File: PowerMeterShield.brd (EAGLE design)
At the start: 71.1 x 53.3 mm, 35 parts, among them U1 INA170EA/2K5, U2 THS4521, U3 INA138, U4 ADUM1250ARZ, U5 MCP3426A0-E/SN, U6 ISL21080

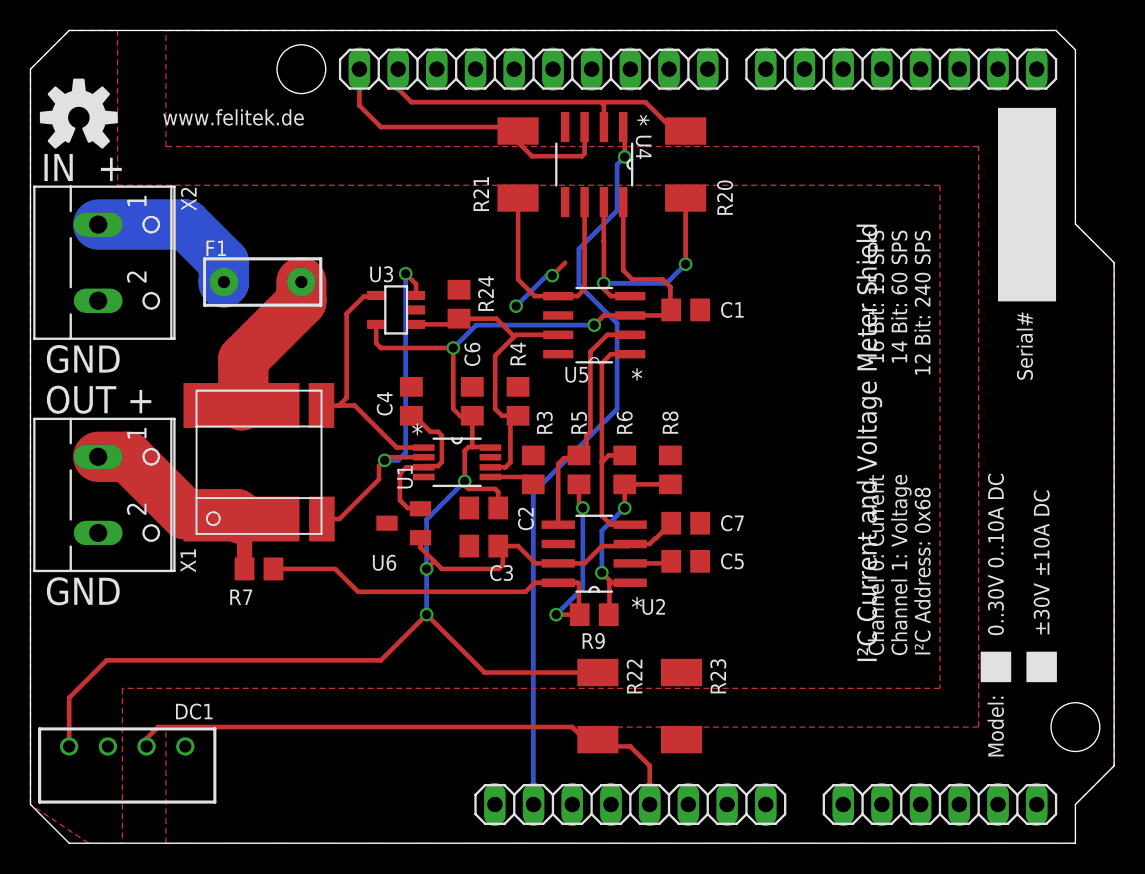
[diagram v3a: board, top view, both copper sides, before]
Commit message: In/Out Sockets conflict with some Arduino's USB/Power jacks, added keepout regions and moved the jacks Reworked the traces from the inputs/outputs to be polygons, thanks moemoe!
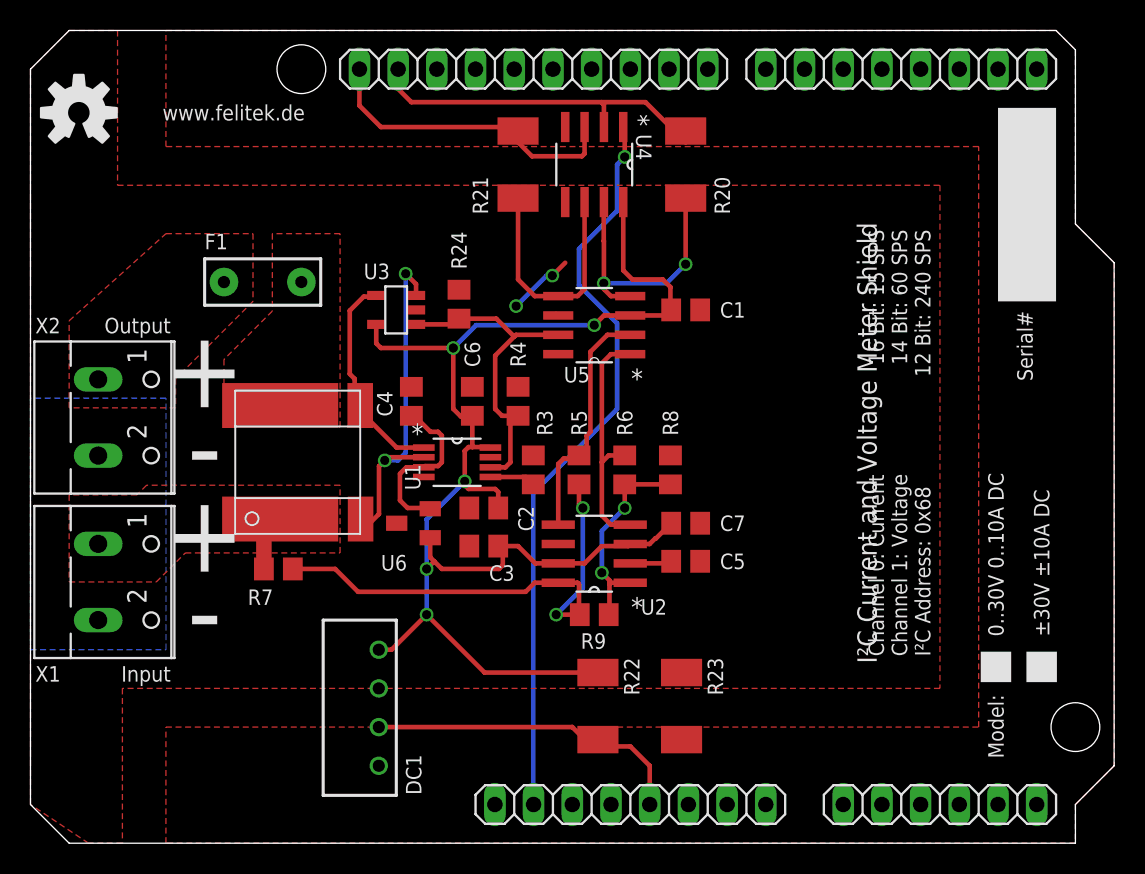
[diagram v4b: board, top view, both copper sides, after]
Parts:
- moved DC1 16.7 mm to (22.9, 8.89), turned to 90 degrees
- moved X2 10.2 mm to (5.71, 27.9)
- moved X1 5.71 mm to (5.71, 17.1)
- moved R1 2.54 mm to (17.5, 25.0)
- moved R7 1.27 mm to (16.3, 18.0)
- moved U6 0.64 mm to (25.1, 21.0)
- moved U$1 0.32 mm to (3.17, 47.9)
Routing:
- net +5V/2: track 119.7 -> 94.6 mm
- net +5V: track 38.1 -> 22.0 mm
- net V_MEAS: track 14.5 -> 3.07 mm
- net VIN_MEAS: track 10.6 -> 0.00 mm
- net N$3: track 9.73 -> 0.00 mm
- net CURRENT-: track 16.5 -> 14.6 mm
- net N$2: track 33.9 -> 32.6 mm
- net CURRENT+: track 23.9 -> 23.0 mm
- net REF: track 10.7 -> 11.3 mm
- added copper zone on layer 16, net GNDI
- added copper zone on layer 1, net N$3
- added copper zone on layer 1, net VIN_MEAS
- added copper zone on layer 1, net V_MEAS
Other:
- board text added: "+"
- board text added: "-"
- board text added: "Input"
- board text added: "Output"
- board text removed: "GND"
- board text removed: "IN +"
- board text removed: "OUT +"

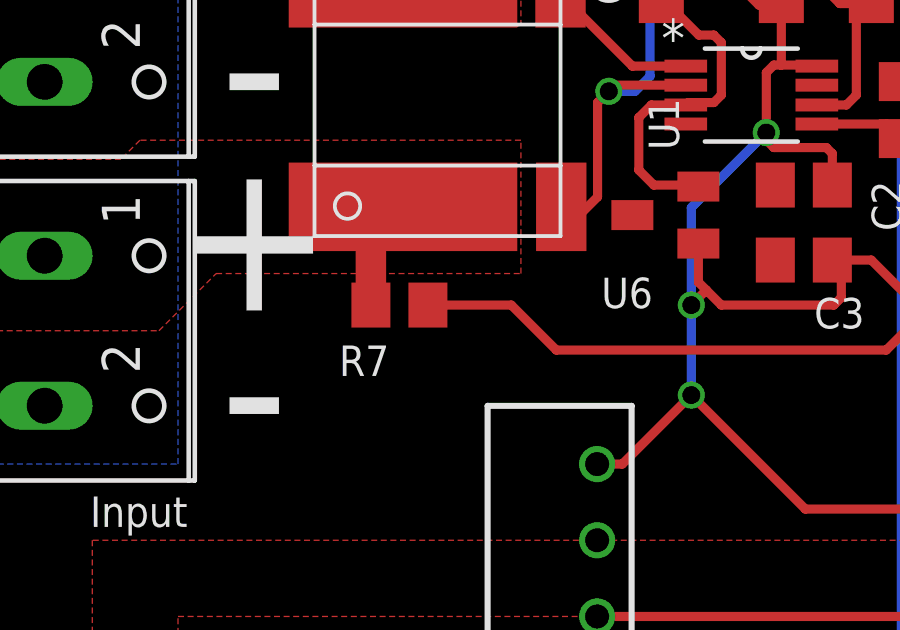
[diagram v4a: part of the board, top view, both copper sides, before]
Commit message: Made "Isolate" for the trace-replacement polygons higher
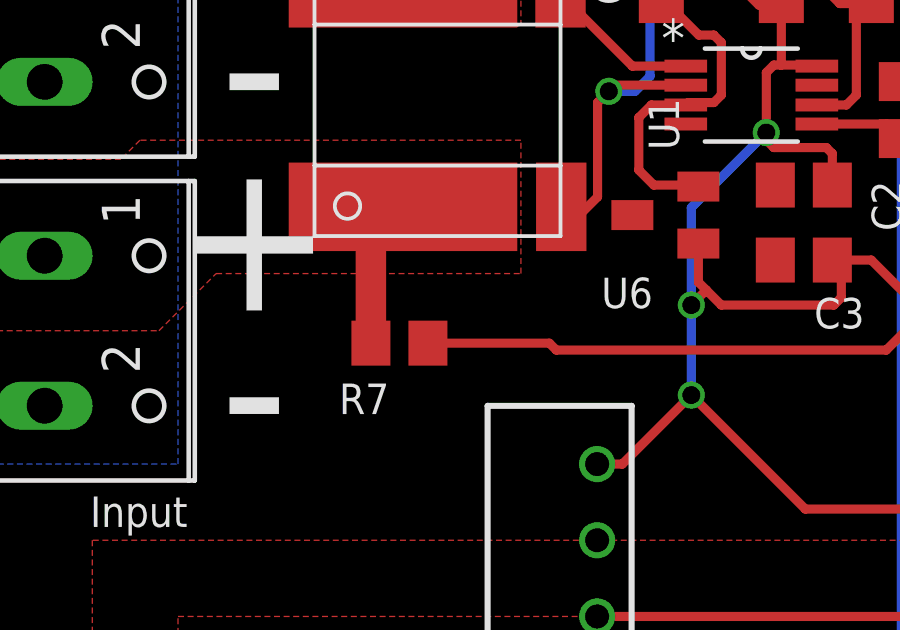
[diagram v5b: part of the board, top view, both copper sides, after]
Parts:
- moved R7 1.27 mm to (16.3, 16.7)
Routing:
- net V_MEAS: track 3.07 -> 4.34 mm
- net N$2: track 32.6 -> 32.1 mm
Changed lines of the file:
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@@
 <attribute name="NAME" x="39" y="26.75" size="1.016" layer="25" rot="R90" align="center-left"/>
 </element>
-<element name="R7" library="rcl" package="R0805" value="6.04M" x="16.27" y="18" smashed="yes">
-<attribute name="NAME" x="14.26" y="16.145" size="1.016" layer="25" align="center-left"/>
+<element name="R7" library="rcl" package="R0805" value="6.04M" x="16.27" y="16.73" smashed="yes">
+<attribute name="NAME" x="14.26" y="14.875" size="1.016" layer="25" align="center-left"/>
 </element>
 <element name="R9" library="rcl" package="R0805" value="412k" x="37" y="15" smashed="yes" rot="R180">
@@
 <contactref element="X2" pad="1"/>
 <contactref element="F1" pad="P$2"/>
-<polygon width="0.3048" layer="1" isolate="0.254">
+<polygon width="0.3048" layer="1" isolate="0.4064">
 <vertex x="14.605" y="40.005"/>
 <vertex x="14.605" y="35.56"/>
@@
 <contactref element="R1" pad="I2"/>
 <contactref element="R7" pad="1"/>
-<wire x1="15.32" y1="18" x2="15.32" y2="21.075" width="1.016" layer="1"/>
-<polygon width="0.3048" layer="1" thermals="no">
+<wire x1="15.32" y1="16.73" x2="15.32" y2="21.075" width="1.016" layer="1"/>
+<polygon width="0.3048" layer="1" isolate="0.4064" thermals="no">
 <vertex x="20.32" y="19.05"/>
 <vertex x="20.32" y="23.495"/>
@@
 <contactref element="X1" pad="2"/>
 <contactref element="X2" pad="2"/>
-<polygon width="0.4064" layer="1" rank="3">
+<polygon width="0.4064" layer="1" orphans="yes" rank="3">
 <vertex x="0" y="2.54"/>
 <vertex x="0" y="50.8"/>
@@
 <wire x1="33.095" y1="17.095" x2="32.5" y2="16.5" width="0.3048" layer="1"/>
 <wire x1="32.5" y1="16.5" x2="21.5" y2="16.5" width="0.3048" layer="1"/>
-<wire x1="21.5" y1="16.5" x2="20" y2="18" width="0.3048" layer="1"/>
-<wire x1="20" y1="18" x2="17.22" y2="18" width="0.3048" layer="1"/>
+<wire x1="21.5" y1="16.5" x2="21.27" y2="16.73" width="0.3048" layer="1"/>
+<wire x1="21.27" y1="16.73" x2="17.22" y2="16.73" width="0.3048" layer="1"/>
 <wire x1="36" y1="23.55" x2="36" y2="22.25" width="0.3048" layer="1"/>
 <wire x1="36" y1="22.25" x2="36.25" y2="22" width="0.3048" layer="1"/>
@@
 <contactref element="R1" pad="I1"/>
 <contactref element="F1" pad="P$1"/>
-<polygon width="0.3048" layer="1" thermals="no" rank="2">
+<polygon width="0.3048" layer="1" isolate="0.4064" thermals="no" rank="2">
 <vertex x="15.875" y="40.005"/>
 <vertex x="15.875" y="34.925"/>

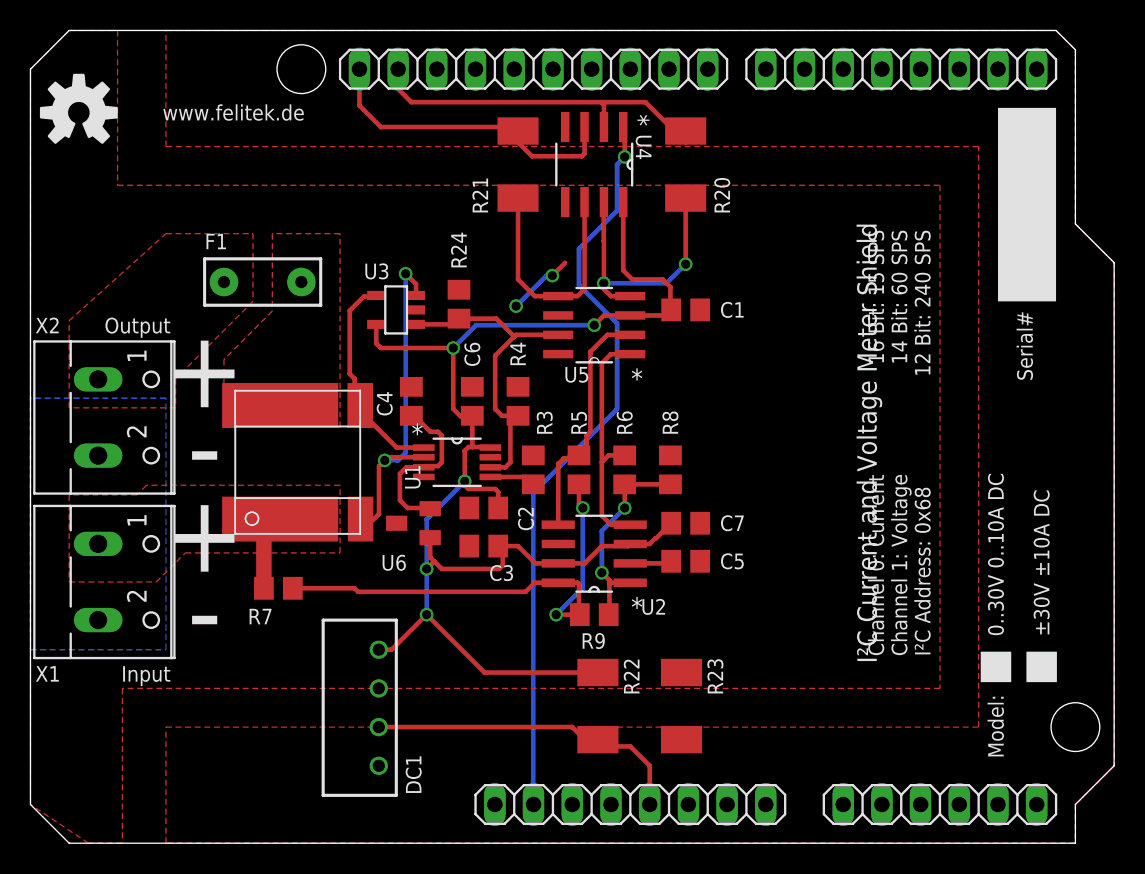
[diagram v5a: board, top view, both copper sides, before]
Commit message: Added SMD DC-DC converter to match height of the shield headers (old one was 10mm high, new one is only 6.3mm high) Added silkscreen for the arduino headers
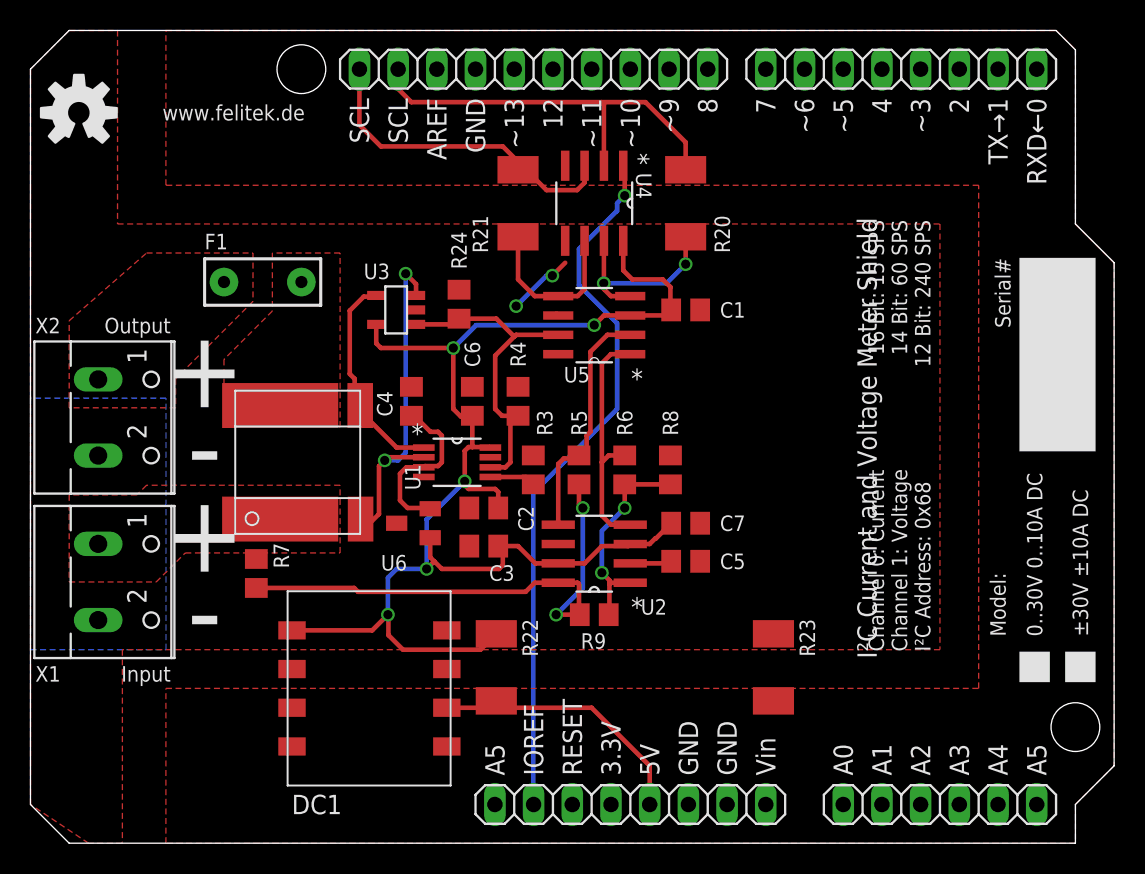
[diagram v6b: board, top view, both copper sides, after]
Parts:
- DC1: value VA-0505S -> R1SE; device dc-dc-converter:4SIL -> R1SE:R1SE
- moved R22 7.13 mm to (30.6, 11.5)
- moved R23 6.55 mm to (48.8, 11.5)
- moved R20 2.54 mm to (43.0, 42.0)
- moved R21 2.54 mm to (32.0, 42.0)
- moved U4 2.54 mm to (37.0, 42.0)
- moved R7 1.74 mm to (14.8, 17.7), turned to 270 degrees
- moved DC1 1.42 mm to (22.2, 10.2)
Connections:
- net +5V/2: now also DC1.5; no longer DC1.4
- net GNDI: now also DC1.4; no longer DC1.3
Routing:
- net SCLI: track 16.1 -> 11.0 mm
- net SDAI: track 17.9 -> 12.8 mm
- net V_MEAS: track 4.34 -> 0.00 mm
- net +5V: track 22.0 -> 17.9 mm
- net SDA: track 24.1 -> 27.7 mm
- net IOREF: track 49.1 -> 46.5 mm
- net N$2: track 32.1 -> 34.5 mm
- net +5V/2: track 94.6 -> 93.4 mm
- net SCL: track 21.1 -> 22.1 mm
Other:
- board text added: "12"
- board text added: "2"
- board text added: "3.3V"
- board text added: "4"
- board text added: "5V"
- board text added: "7"
- board text added: "8"
- board text added: "A0"
- board text added: "A1"
- board text added: "A2"
- board text added: "A3"
- board text added: "A4"
- board text added: "A5"
- board text added: "AREF"
- board text added: "GND"
- board text added: "IOREF"
- board text added: "RESET"
- board text added: "RXD←0"
- board text added: "SCL"
- board text added: "TX→1"
- board text added: "Vin"
- board text added: "~10"
- board text added: "~11"
- board text added: "~13"
- board text added: "~3"
- board text added: "~5"
- board text added: "~6"
- board text added: "~9"
